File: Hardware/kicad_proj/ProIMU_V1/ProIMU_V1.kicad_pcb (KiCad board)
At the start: 2 copper layers, 50 x 50 mm, 66 parts, among them IC1 MP2731GQC-0000-Z, J1 Conn_02x03_Counter_Clockwise, J4 502570-0893, Q1 2SC4213, U1 ADM101E, U10 STM32F412RETx, U2 TJA1051T-3, U3 LTC2942-1, U4 AIR602, U5 BMP280, U6 MPU-9250, U7 TPS54308, U9 L80-M39

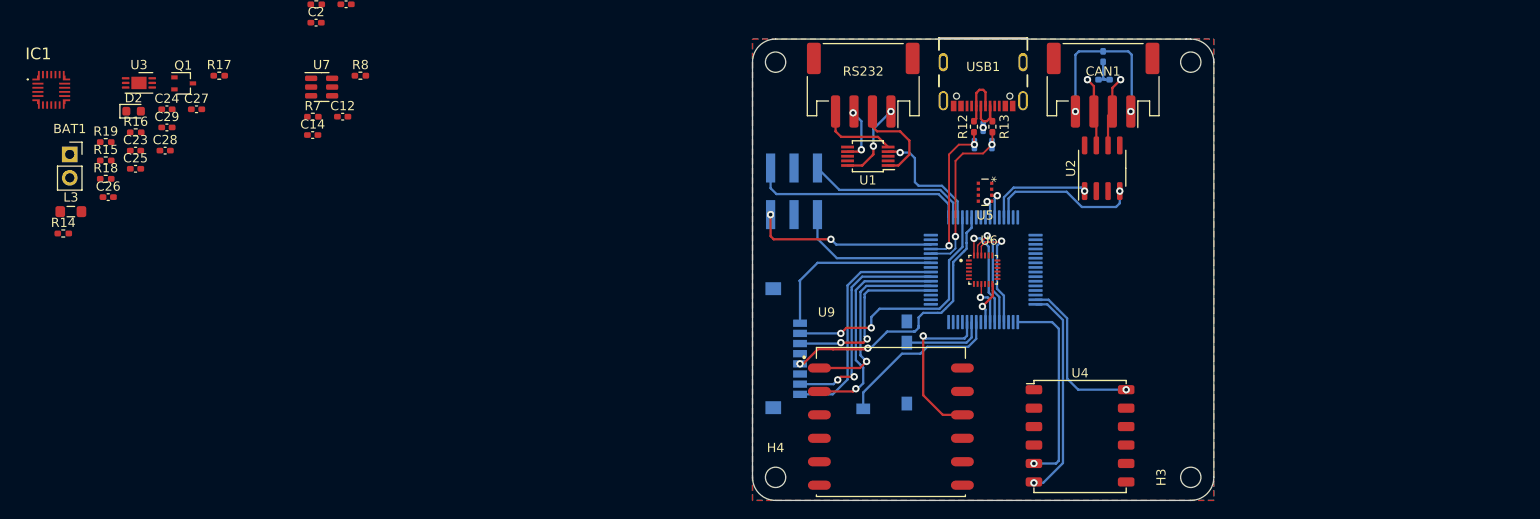
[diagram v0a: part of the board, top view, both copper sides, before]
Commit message: Updated schematic and layout
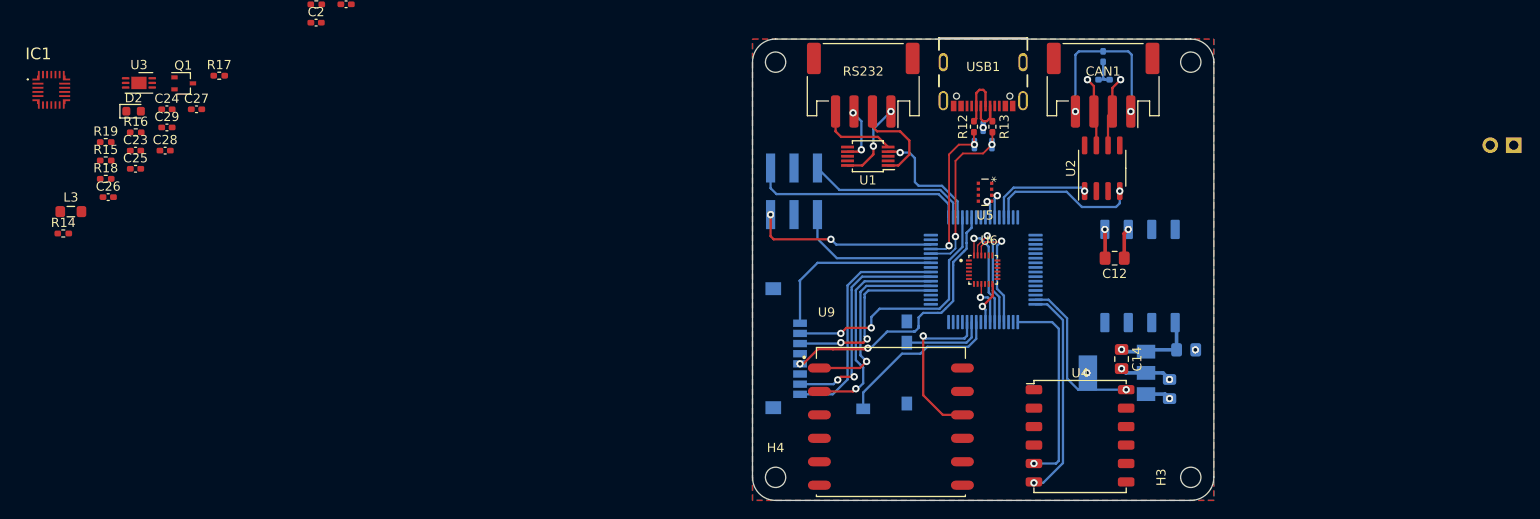
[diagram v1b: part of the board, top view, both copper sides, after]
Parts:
- removed R7, R8: 10K, Resistor_SMD:R_0402_1005Metric_Pad0.72x0.64mm_HandSolder
- added C13: C, Capacitor_SMD:C_0805_2012Metric_Pad1.18x1.45mm_HandSolder, B.Cu at (170.5, 113.7)
- added C15: C, Capacitor_SMD:C_0805_2012Metric_Pad1.18x1.45mm_HandSolder, B.Cu at (168.7, 117.9)
- added PS1: PDP1-S5-S5-M-TR, footprints:CONV_PDP1-S5-S5-M-TR, B.Cu at (165.5, 105.7)
- BAT1: footprint Connector_PinSocket_2.54mm:PinSocket_1x02_P2.54mm_Vertical -> Connector_PinHeader_2.54mm:PinHeader_1x02_P2.54mm_Vertical; moved to B.Cu
- C12, C14: value 1uF -> C; footprint Capacitor_SMD:C_0402_1005Metric_Pad0.74x0.62mm_HandSolder -> Capacitor_SMD:C_0805_2012Metric_Pad1.18x1.45mm_HandSolder
- U7: value TPS54308 -> SPX2920M3-3.3_SOT223; footprint Package_TO_SOT_SMD:SOT-23-6 -> Package_TO_SOT_SMD:SOT-223-3_TabPin2; moved to B.Cu
- moved BAT1 156.5 mm to (206.0, 91.5), turned to 90 degrees
- moved U7 91.6 mm to (163.0, 116.2), turned to 180 degrees
- moved C14 91.0 mm to (163.5, 114.7), turned to -90 degrees
- moved C12 85.1 mm to (162.8, 103.8), turned to 180 degrees
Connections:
- BAT1 pad 1: Net-(BAT1-Pad1) -> unconnected-(BAT1-Pad1)
- BAT1 pad 2: Net-(BAT1-Pad2) -> unconnected-(BAT1-Pad2)
- C12 pad 1: Net-(C12-Pad1) -> VDD
- C12 pad 2: Net-(C12-Pad2) -> GND1
- C14 pad 1: +3V3 -> +5V
- C26 pad 1: Net-(BAT1-Pad1) -> Net-(C26-Pad1)
- C29 pad 1: Net-(BAT1-Pad1) -> Net-(C26-Pad1)
- C5 pad 1: Net-(CAN1-Pad1) -> Net-(C5-Pad1)
- CAN1 pad 1: Net-(CAN1-Pad1) -> VDD
- CAN1 pad 4: Net-(CAN1-Pad1) -> Net-(C5-Pad1)
- IC1 pad 17: Net-(BAT1-Pad1) -> Net-(C26-Pad1)
- R15 pad 1: Net-(BAT1-Pad2) -> unconnected-(R15-Pad1)
- U7 pad 1: GND -> +5V
- U7 pad 2: Net-(C12-Pad2) -> GND
- U7 pad 3: VDD -> +3V3
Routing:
- net Net-(CAN1-Pad1): track 18.7 -> 0.00 mm, vias 2 -> 0
- net Net-(C5-Pad1): track 0.00 -> 18.7 mm, vias 0 -> 2
- net +5V: track 0.00 -> 9.16 mm, vias 0 -> 1
- net GND: track 0.04 -> 5.86 mm, vias 1 -> 5
- net VDD: track 0.00 -> 3.30 mm, vias 0 -> 1
- net GND1: track 0.00 -> 3.13 mm, vias 0 -> 1
- net +3V3: track 0.00 -> 2.75 mm, vias 0 -> 1

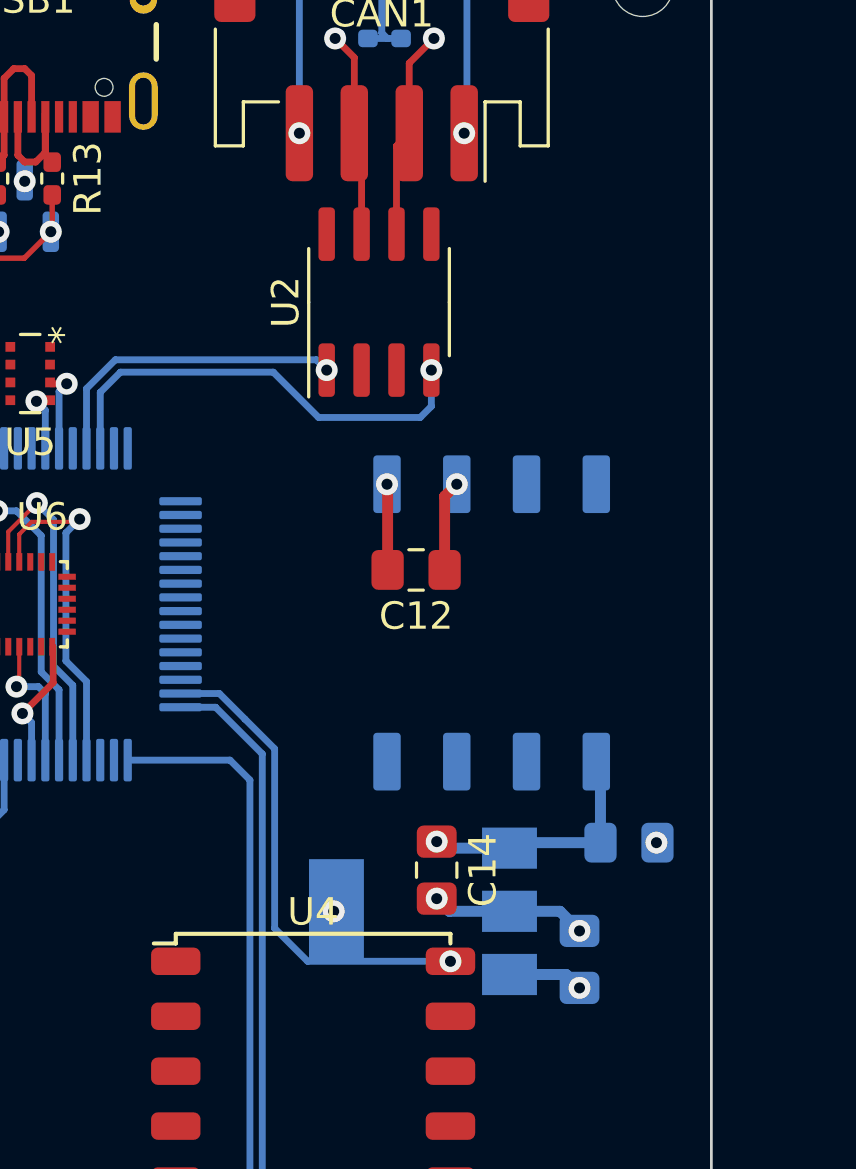
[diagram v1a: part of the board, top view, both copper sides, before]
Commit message: Updated schematic and layout
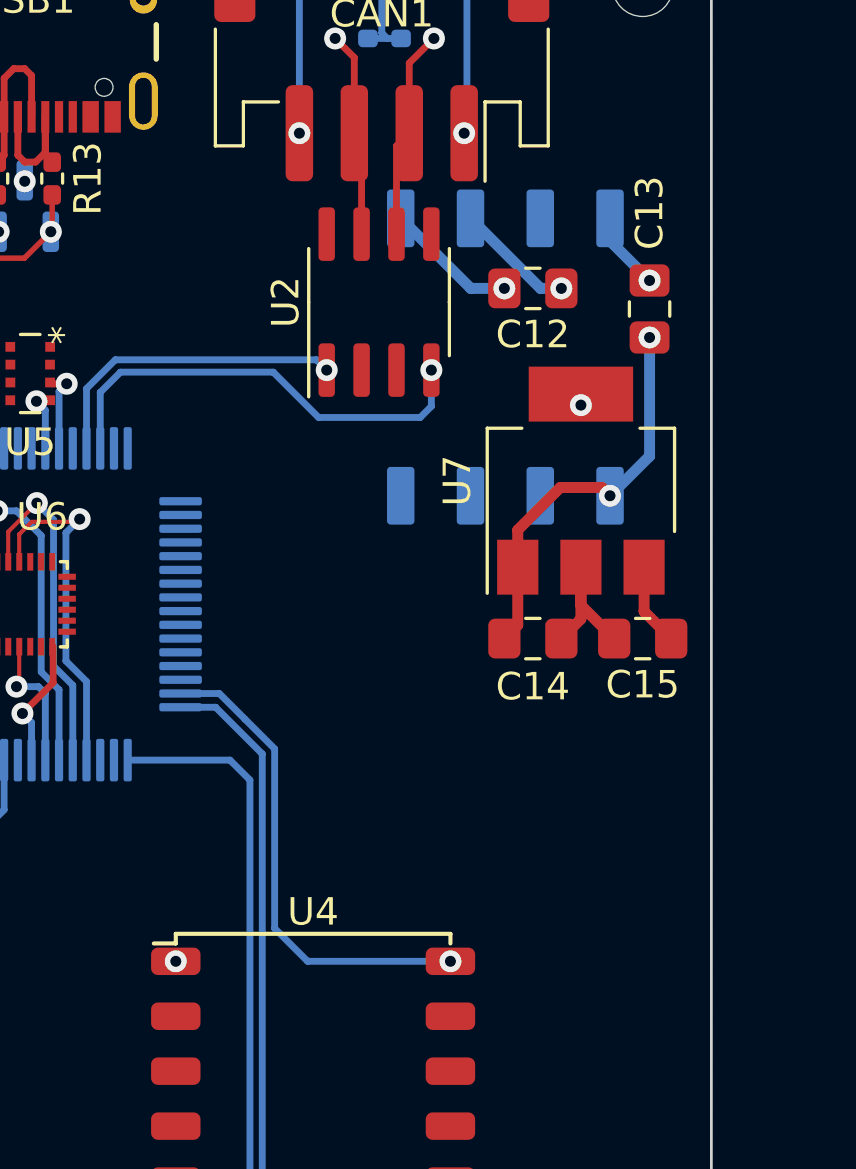
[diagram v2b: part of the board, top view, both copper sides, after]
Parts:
- C13, C15, U7: moved to F.Cu
- moved C13 19.4 mm to (171.2, 94.2), turned to 90 degrees
- moved U7 16.7 mm to (168.8, 100.5), turned to 90 degrees
- moved C15 11.9 mm to (171.0, 106.2), turned to 180 degrees
- moved C12 11.1 mm to (167.0, 93.5)
- moved PS1 9.69 mm to (166.0, 96.0)
- moved C14 9.13 mm to (167.0, 106.2), turned to 0 degrees
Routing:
- net +5V: track 9.16 -> 14.6 mm, vias 1 -> 2
- net GND: track 5.86 -> 9.29 mm, vias 5 -> 4
- net GND1: track 3.13 -> 4.83 mm
- net VDD: track 3.30 -> 4.36 mm
- net +3V3: track 2.75 -> 3.01 mm, vias 1 -> 0

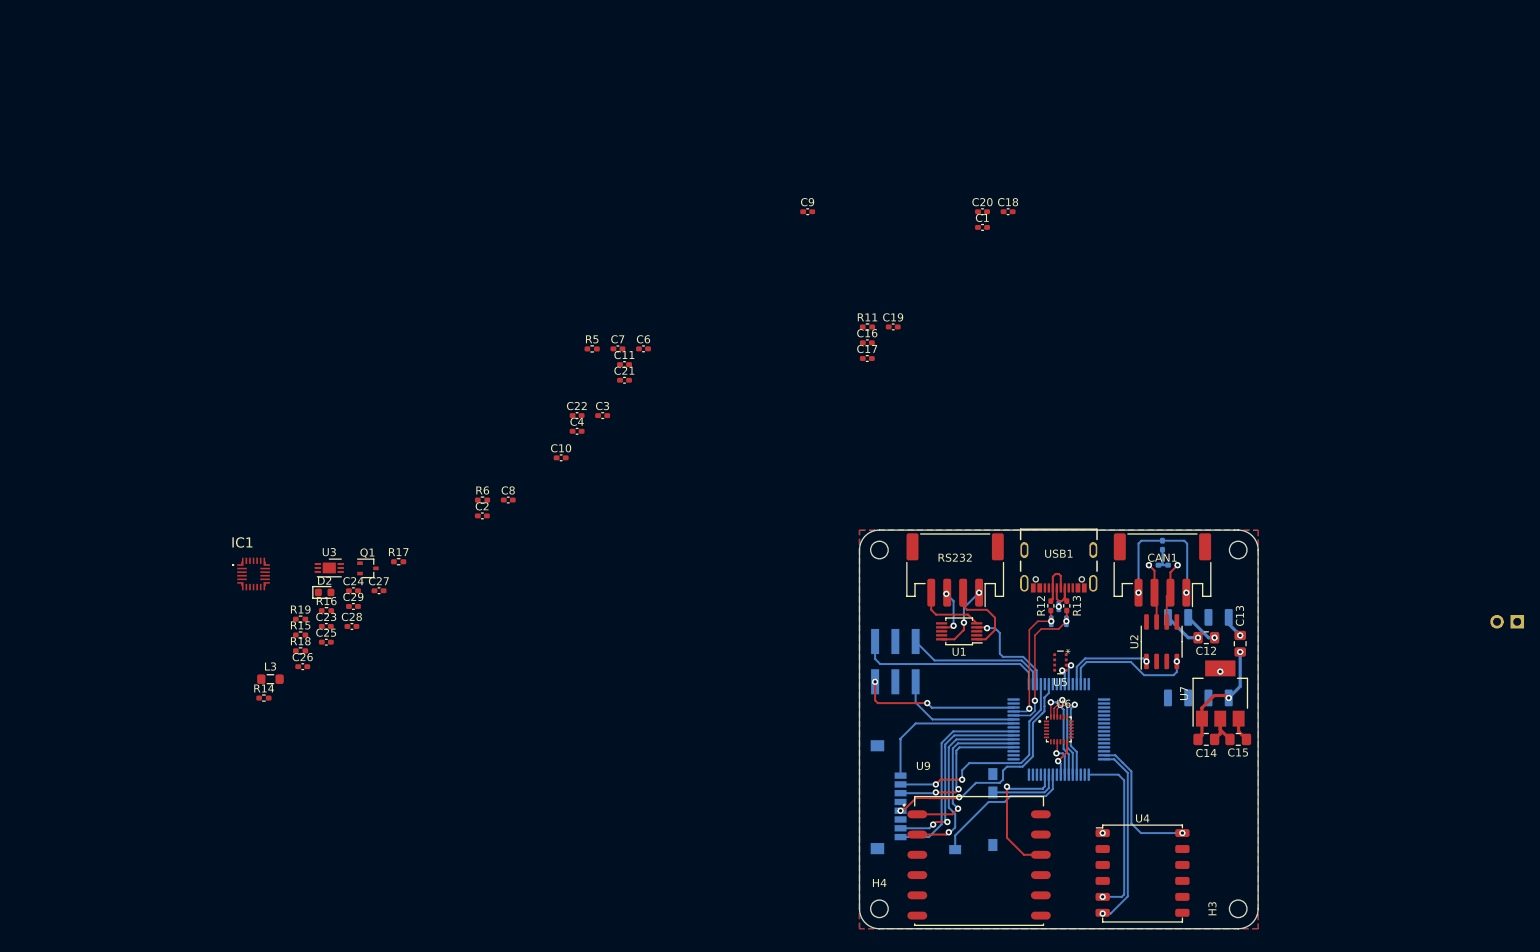
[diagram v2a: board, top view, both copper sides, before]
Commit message: Updated schematic and layout
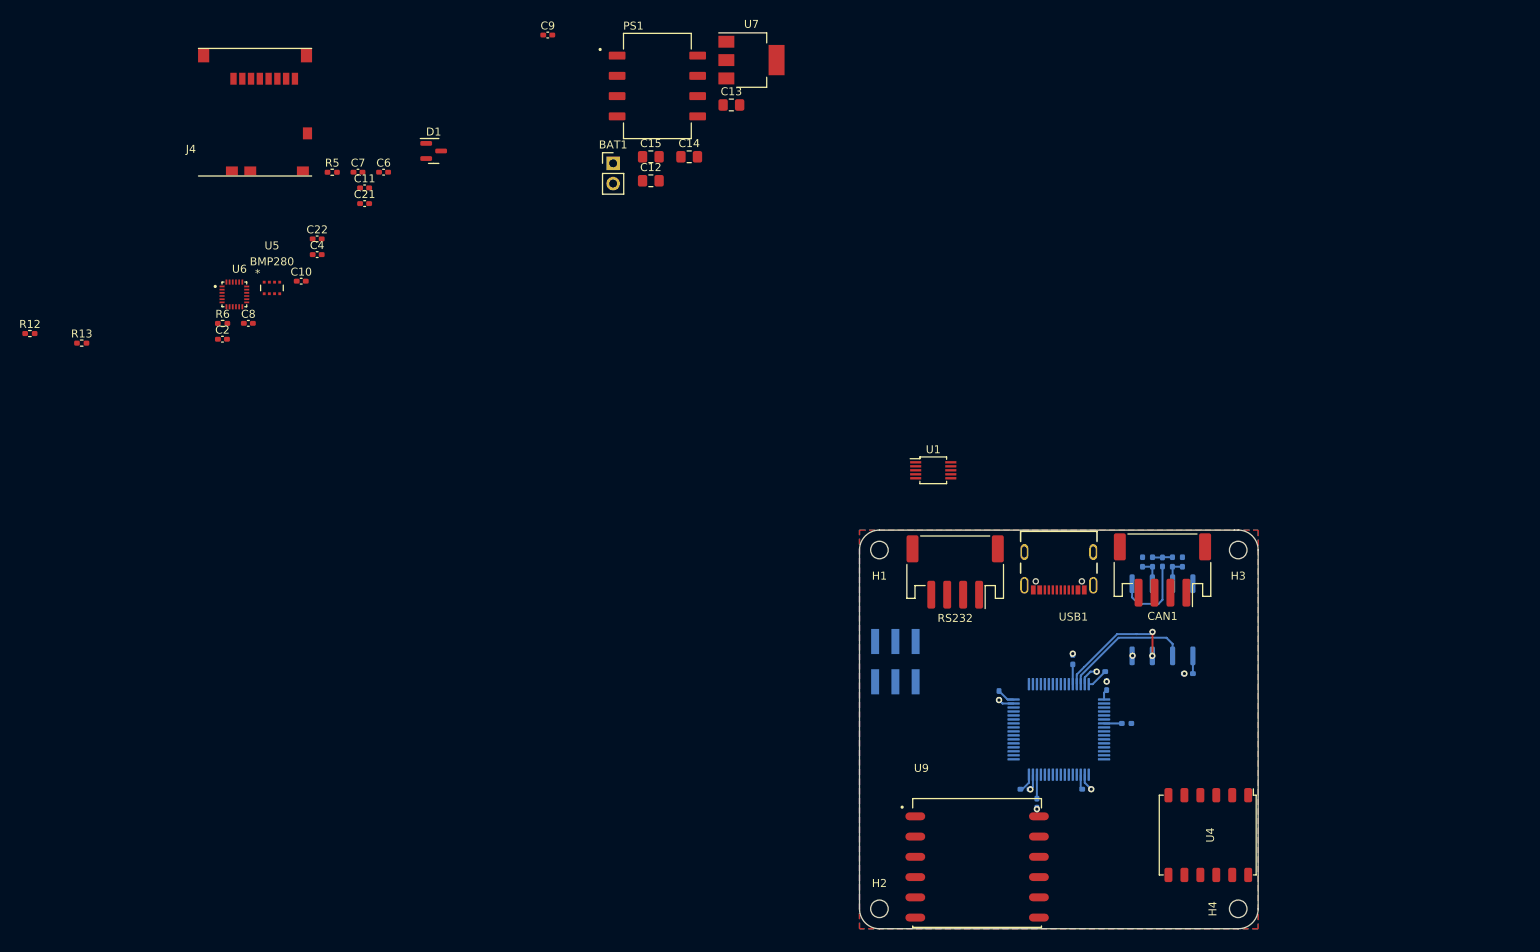
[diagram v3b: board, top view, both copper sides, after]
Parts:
- removed C23, C25, C26, C28, C29: 1uF, Capacitor_SMD:C_0402_1005Metric_Pad0.74x0.62mm_HandSolder
- removed C24, C27: 10uF, Capacitor_SMD:C_0402_1005Metric_Pad0.74x0.62mm_HandSolder
- removed D2: LED, LED_SMD:LED_0603_1608Metric
- removed IC1: MP2731GQC-0000-Z, footprints:MP2731GQC0000Z
- removed L3: 1.0uH, Inductor_SMD:L_0805_2012Metric_Pad1.05x1.20mm_HandSolder
- removed Q1: 2SC4213, Package_TO_SOT_SMD:SOT-323_SC-70
- removed R14, R17, R19: 10K, Resistor_SMD:R_0402_1005Metric_Pad0.72x0.64mm_HandSolder
- removed R15, R16, R18: 1K, Resistor_SMD:R_0402_1005Metric_Pad0.72x0.64mm_HandSolder
- removed U3: LTC2942-1, Package_DFN_QFN:DFN-6-1EP_3x2mm_P0.5mm_EP1.65x1.35mm
- added R3: 10K, Resistor_SMD:R_0402_1005Metric_Pad0.72x0.64mm_HandSolder, B.Cu at (157.0, 104.2)
- added R4: 2.2K, Resistor_SMD:R_0402_1005Metric_Pad0.72x0.64mm_HandSolder, B.Cu at (164.0, 84.0)
- added R7: 2.2K, Resistor_SMD:R_0402_1005Metric_Pad0.72x0.64mm_HandSolder, B.Cu at (159.0, 84.0)
- BAT1, D1, J4, PS1: moved to F.Cu
- C1, C16, C17, C18, C19, C20, C3, R11: moved to B.Cu
- U2: value TJA1051T-3 -> ISO1050DUB; footprint Package_SO:SOIC-8_3.9x4.9mm_P1.27mm -> Package_SO:SOP-8_6.62x9.15mm_P2.54mm; moved to B.Cu
- moved R12 132.5 mm to (19.4, 55.4), turned to 0 degrees
- moved R13 127.9 mm to (25.9, 56.5), turned to 0 degrees
- moved BAT1 127.1 mm to (92.6, 34.0), turned to 0 degrees
- moved J4 121.0 mm to (47.7, 27.6), turned to 0 degrees
- moved U6 116.9 mm to (45.1, 50.4)
- moved U5 109.5 mm to (49.8, 49.6), turned to 0 degrees
- moved C15 103.8 mm to (97.3, 33.2), turned to 0 degrees
- moved U7 98.8 mm to (110.0, 21.1), turned to 0 degrees
- moved PS1 98.7 mm to (98.2, 24.3), turned to 0 degrees
- moved C14 97.7 mm to (102.1, 33.2)
- moved D1 97.6 mm to (70.1, 32.5), turned to 0 degrees
- moved C13 92.9 mm to (107.4, 26.7), turned to 0 degrees
- moved C12 90.2 mm to (97.3, 36.2), turned to 0 degrees
- moved C3 72.6 mm to (161.5, 84.0), turned to 90 degrees
- moved C18 72.5 mm to (144.2, 112.5)
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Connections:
- net /Battery/D+ renamed /MCU/USB-
- net /Battery/D- renamed /MCU/USB+
- C3 pad 1: GND -> GND1
- C3 pad 2: +5V -> Net-(R1-Pad2)
- C5 pad 1: Net-(C5-Pad1) -> GND
- C5 pad 2: Net-(C5-Pad2) -> +3V3
- CAN1 pad 4: Net-(C5-Pad1) -> GND1
- R1 pad 1: Net-(CAN1-Pad2) -> Net-(R1-Pad1)
- R1 pad 2: Net-(C5-Pad2) -> Net-(R1-Pad2)
- R2 pad 1: Net-(C5-Pad2) -> Net-(R1-Pad2)
- R2 pad 2: Net-(CAN1-Pad3) -> Net-(R2-Pad2)
- U2 pad 1: /MCU/CAN1_TX -> +3V3
- U2 pad 2: GND -> /MCU/CAN1_RX
- U2 pad 3: +5V -> /MCU/CAN1_TX
- U2 pad 4: /MCU/CAN1_RX -> GND
- U2 pad 5: +3V3 -> GND1
- U2 pad 6: Net-(CAN1-Pad2) -> Net-(R2-Pad2)
- U2 pad 7: Net-(CAN1-Pad3) -> Net-(R1-Pad1)
- U2 pad 8: GND -> VDD
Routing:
- net /MCU/SDCARD_SDIO_CMD: track 30.0 -> 0.00 mm, vias 2 -> 0
- net /MCU/SDCARD_SDIO_D3: track 27.8 -> 0.00 mm, vias 2 -> 0
- net /MCU/SDCARD_SDIO_D1: track 25.6 -> 0.00 mm
- net /MCU/SDCARD_SDIO_D0: track 25.1 -> 0.00 mm, vias 2 -> 0
- net /MCU/GPS_UART6_RX: track 24.1 -> 0.00 mm, vias 1 -> 0
- net /MCU/DEBUG_SWCLK: track 23.6 -> 0.00 mm
- net /MCU/WIFI_UART2_TX: track 23.3 -> 0.00 mm, vias 1 -> 0
- net /MCU/WIFI_UART2_RX: track 21.9 -> 0.00 mm, vias 1 -> 0
- net /MCU/GPS_UART6_TX: track 21.1 -> 0.00 mm, vias 1 -> 0
- net /MCU/DEBUG_SWDIO: track 20.1 -> 0.00 mm, vias 2 -> 0
- net /MCU/SDCARD_SDIO_CLK: track 19.8 -> 0.00 mm, vias 2 -> 0
- net /MCU/SDCARD_SDIO_D2: track 19.7 -> 0.00 mm
- net Net-(C5-Pad1): track 18.7 -> 0.00 mm, vias 2 -> 0
- net /MCU/USB-: track 18.4 -> 0.00 mm, vias 2 -> 0
- net /MCU/SDCARD_DET_LEVEL: track 18.2 -> 0.00 mm
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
